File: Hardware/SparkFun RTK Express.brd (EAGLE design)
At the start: 68.2 x 110.1 mm, 166 parts, among them J13 Internal, J16 microSD, J17 Qwiic Right Angle, J3 USB Female Type C Connector, J4 External, J5 USB Female Type C Connector, Q1 SIL2308-TP, Q2 MBT3904DW1T1, U1 74HC4052D, U10 MCP73833, U13 LIS2DH12, U2 AP2112K-3.3, U3 U-BLOX_ZED-F9P, U4 STLQ015-3.3V, U5 ESP-WROOM-3232D-NARROW, U6 CH340C, U7 MAX17048

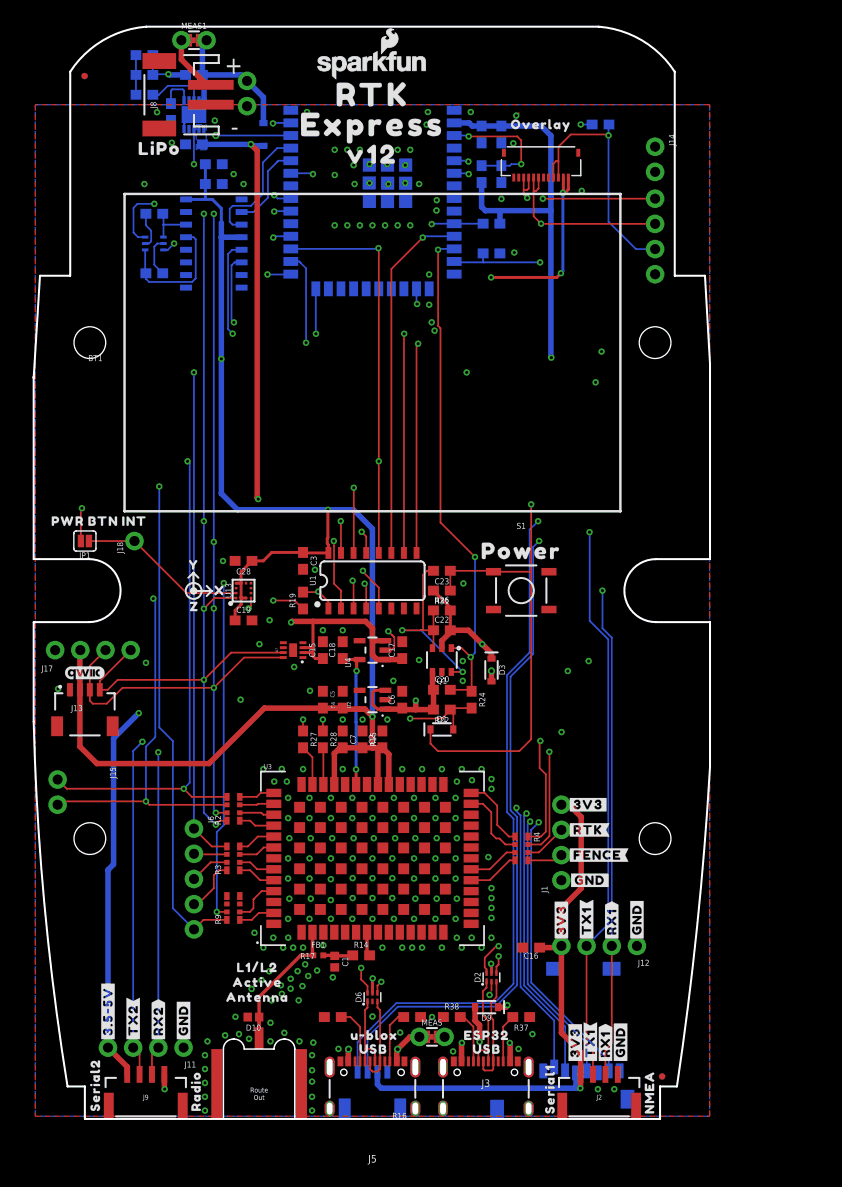
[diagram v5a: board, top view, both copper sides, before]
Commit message: Move microSD socket further out.
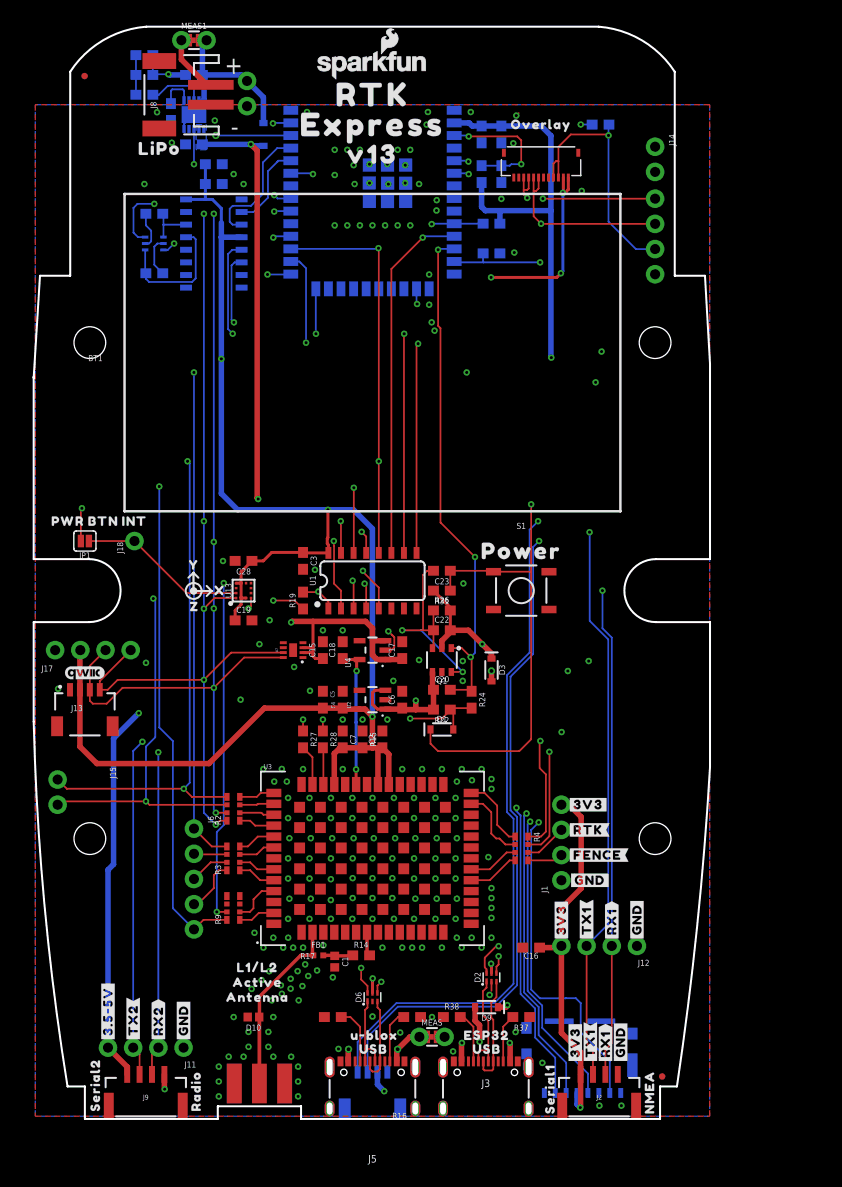
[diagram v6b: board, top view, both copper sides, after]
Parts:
- removed U$12: (no value), output:V120
- added U$18, U$19: (no value), output:V130
- E1: device SparkFun-RF:SMA-EDGE-SMD -> SparkFun-RF:SMA-EDGE
- J16: device SparkFun-Connectors:MICRO-SD-SOCKET -> SparkFun-Connectors:MICROSD_TINY
- moved J16 10.5 mm to (55.9, 6.19), turned to 0 degrees
- moved E1 3.53 mm to (23.6, 3.30)
- moved U$83 3.17 mm to (62.9, 11.4)
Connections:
- net 3.3V: now also J16.4; no longer J16.VCC
- net ESP_18/SCK: now also J16.5; no longer J16.SCLK
- net ESP_19/CIPO: now also J16.7; no longer J16.DO/DAT0
- net ESP_23/COPI: now also J16.3; no longer J16.DI/CMD
- net ESP_25/SD_!CS!: now also J16.2; no longer J16.CS/DAT3
- net GND: now also E1.GND@2, E1.GND@3, J16.6, J16.9, J16.GND2, J16.GND4, J16.GND5, J16.GND6; no longer J16.CD1, J16.GND
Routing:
- net GPS_ANT1: track 15.9 -> 25.0 mm
- net ESP_19/CIPO: track 115.7 -> 120.1 mm
- net 3.3V: track 317.2 -> 320.0 mm, vias 6 -> 7
- net ESP_25/SD_!CS!: track 97.3 -> 100.0 mm
- net ESP_18/SCK: track 114.0 -> 116.2 mm
- net ESP_23/COPI: track 120.9 -> 123.2 mm
- net GND: track 18.1 -> 18.3 mm, vias 205 -> 201
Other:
- outline, holes or cut-outs redrawn
- board text removed: "11.9+2.75=14.65mm"
- board text removed: "11.9-3.4=8.5mm actuator length on square button"
- board text removed: "11.9-8=3.9"
- board text removed: "18.5-5-1.6=11.9mm"
- board text removed: "Distance from PCB surface to outer surface of lid:"
- board text removed: "Distance from inner lid to PCB surface:"

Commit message: Remove push pull SD socket. v13 PCB
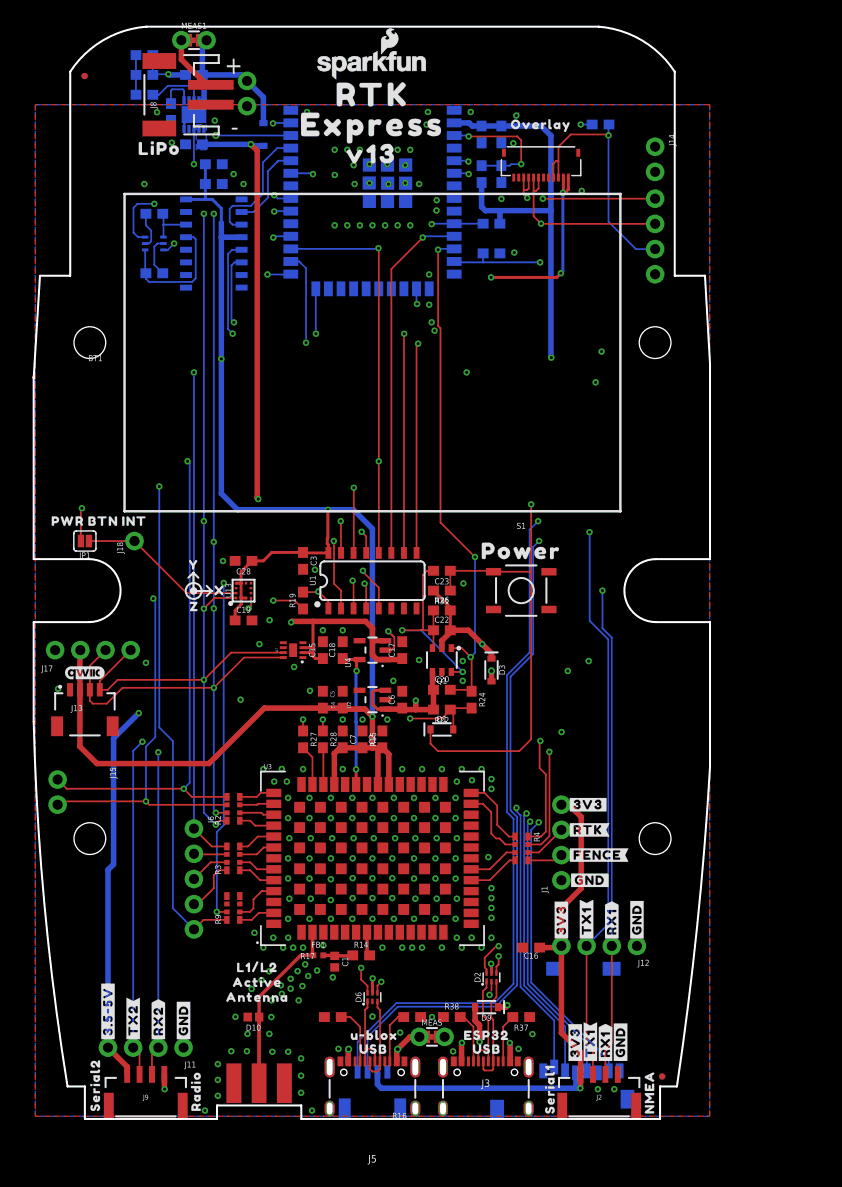
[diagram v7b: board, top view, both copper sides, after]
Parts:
- removed U$19: (no value), output:V130
- J16: device SparkFun-Connectors:MICROSD_TINY -> SparkFun-Connectors:MICRO-SD-SOCKET
- moved J16 10.5 mm to (61.2, 15.3), turned to 180 degrees
- moved U$83 3.17 mm to (62.2, 14.5)
- moved U$18 0.08 mm to (34.9, 97.0)
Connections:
- net 3.3V: now also J16.VCC; no longer J16.4
- net ESP_18/SCK: now also J16.SCLK; no longer J16.5
- net ESP_19/CIPO: now also J16.DO/DAT0; no longer J16.7
- net ESP_23/COPI: now also J16.DI/CMD; no longer J16.3
- net ESP_25/SD_!CS!: now also J16.CS/DAT3; no longer J16.2
- net GND: now also J16.CD1, J16.GND; no longer J16.6, J16.9, J16.GND2, J16.GND4, J16.GND5, J16.GND6
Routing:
- net ESP_19/CIPO: track 120.1 -> 115.7 mm
- net 3.3V: track 320.0 -> 317.2 mm, vias 7 -> 6
- net ESP_25/SD_!CS!: track 100.0 -> 97.3 mm
- net ESP_18/SCK: track 116.2 -> 114.0 mm
- net ESP_23/COPI: track 123.2 -> 120.9 mm
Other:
- outline, holes or cut-outs redrawn
- board text added: "11.9+2.75=14.65mm"
- board text added: "11.9-3.4=8.5mm actuator length on square button"
- board text added: "11.9-8=3.9"
- board text added: "18.5-5-1.6=11.9mm"
- board text added: "Distance from PCB surface to outer surface of lid:"
- board text added: "Distance from inner lid to PCB surface:"

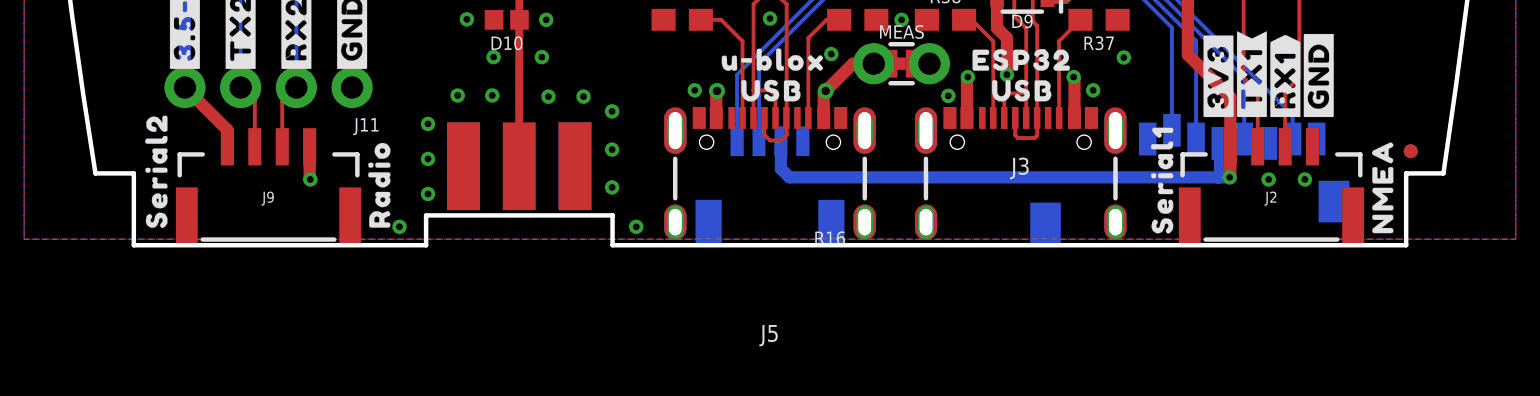
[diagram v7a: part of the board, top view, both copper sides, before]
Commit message: v13 PCB. Add panel. Change from SMD SMA To edge mount SMD to increase strength of connector.
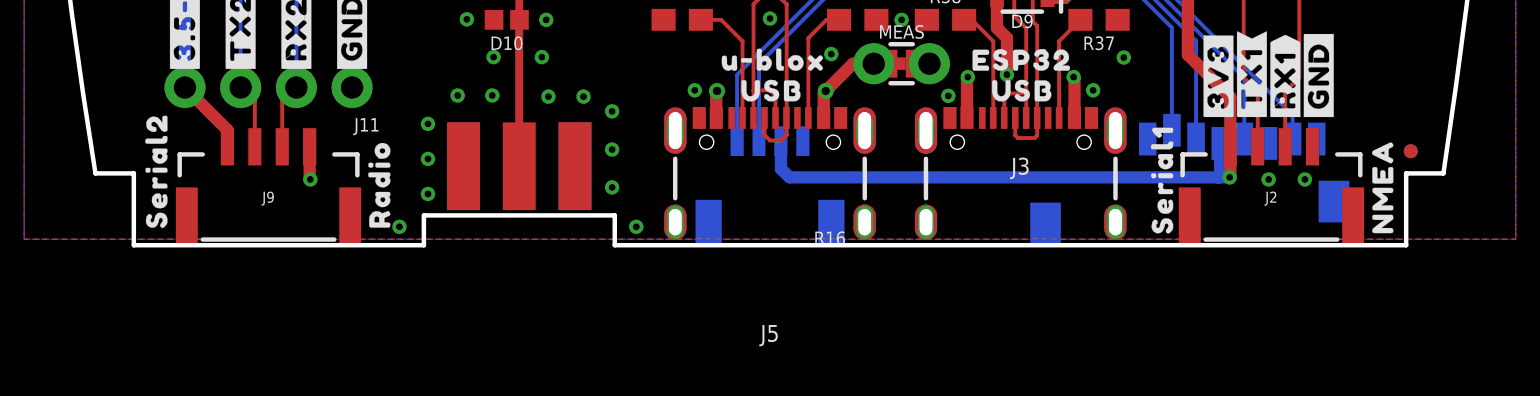
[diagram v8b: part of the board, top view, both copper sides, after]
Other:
- outline, holes or cut-outs redrawn
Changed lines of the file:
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@@
 <setting verticaltext="up"/>
 </settings>
-<grid distance="1" unitdist="mm" unit="mm" style="lines" multiple="1" display="yes" altdistance="0.1" altunitdist="mm" altunit="mm"/>
+<grid distance="0.05" unitdist="inch" unit="inch" style="lines" multiple="1" display="yes" altdistance="0.005" altunitdist="inch" altunit="inch"/>
 <layers>
 <layer number="1" name="Top/Horz" color="4" fill="1" visible="yes" active="yes"/>
@@
 <wire x1="6.425" y1="49.825" x2="6.425" y2="56.175" width="0.2032" layer="20" curve="180"/>
 <wire x1="63.575" y1="49.825" x2="63.575" y2="56.175" width="0.2032" layer="20" curve="-180"/>
-<wire x1="6" y1="-0.275" x2="19.323" y2="-0.275" width="0.2032" layer="20"/>
-<wire x1="27.823" y1="-0.275" x2="64" y2="-0.275" width="0.2032" layer="20"/>
+<wire x1="6" y1="-0.275" x2="19.223" y2="-0.275" width="0.2032" layer="20"/>
+<wire x1="27.923" y1="-0.275" x2="64" y2="-0.275" width="0.2032" layer="20"/>
 <wire x1="6" y1="-0.275" x2="6" y2="3" width="0.2032" layer="20"/>
 <wire x1="6" y1="3" x2="4.25" y2="3" width="0.2032" layer="20"/>
@@
 <wire x1="16.942" y1="54.806" x2="17.45" y2="54.298" width="0.2032" layer="21"/>
 <wire x1="16.942" y1="54.806" x2="16.434" y2="54.298" width="0.2032" layer="21"/>
-<wire x1="27.823" y1="-0.275" x2="27.823" y2="1.084" width="0.2032" layer="20"/>
-<wire x1="27.823" y1="1.084" x2="19.323" y2="1.084" width="0.2032" layer="20"/>
-<wire x1="19.323" y1="1.084" x2="19.323" y2="-0.275" width="0.2032" layer="20"/>
+<wire x1="27.923" y1="-0.275" x2="27.923" y2="1.084" width="0.2032" layer="20"/>
+<wire x1="27.923" y1="1.084" x2="19.223" y2="1.084" width="0.2032" layer="20"/>
+<wire x1="19.223" y1="1.084" x2="19.223" y2="-0.275" width="0.2032" layer="20"/>
 </plain>
 <attributes>
